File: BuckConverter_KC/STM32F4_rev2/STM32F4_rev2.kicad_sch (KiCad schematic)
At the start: 50 parts, among them J1 Screw_Terminal_01x02, J2 SWD, J3 Conn_01x04, J4 Conn_01x04, J5 USB_B_Micro, Q1 AO3401A, SW1 SW_SPDT, U1 MP2359DJ-LF-Z, U2 STM32F405RGTy, U3 USBLC6-2SC6, Y1 16Mhz

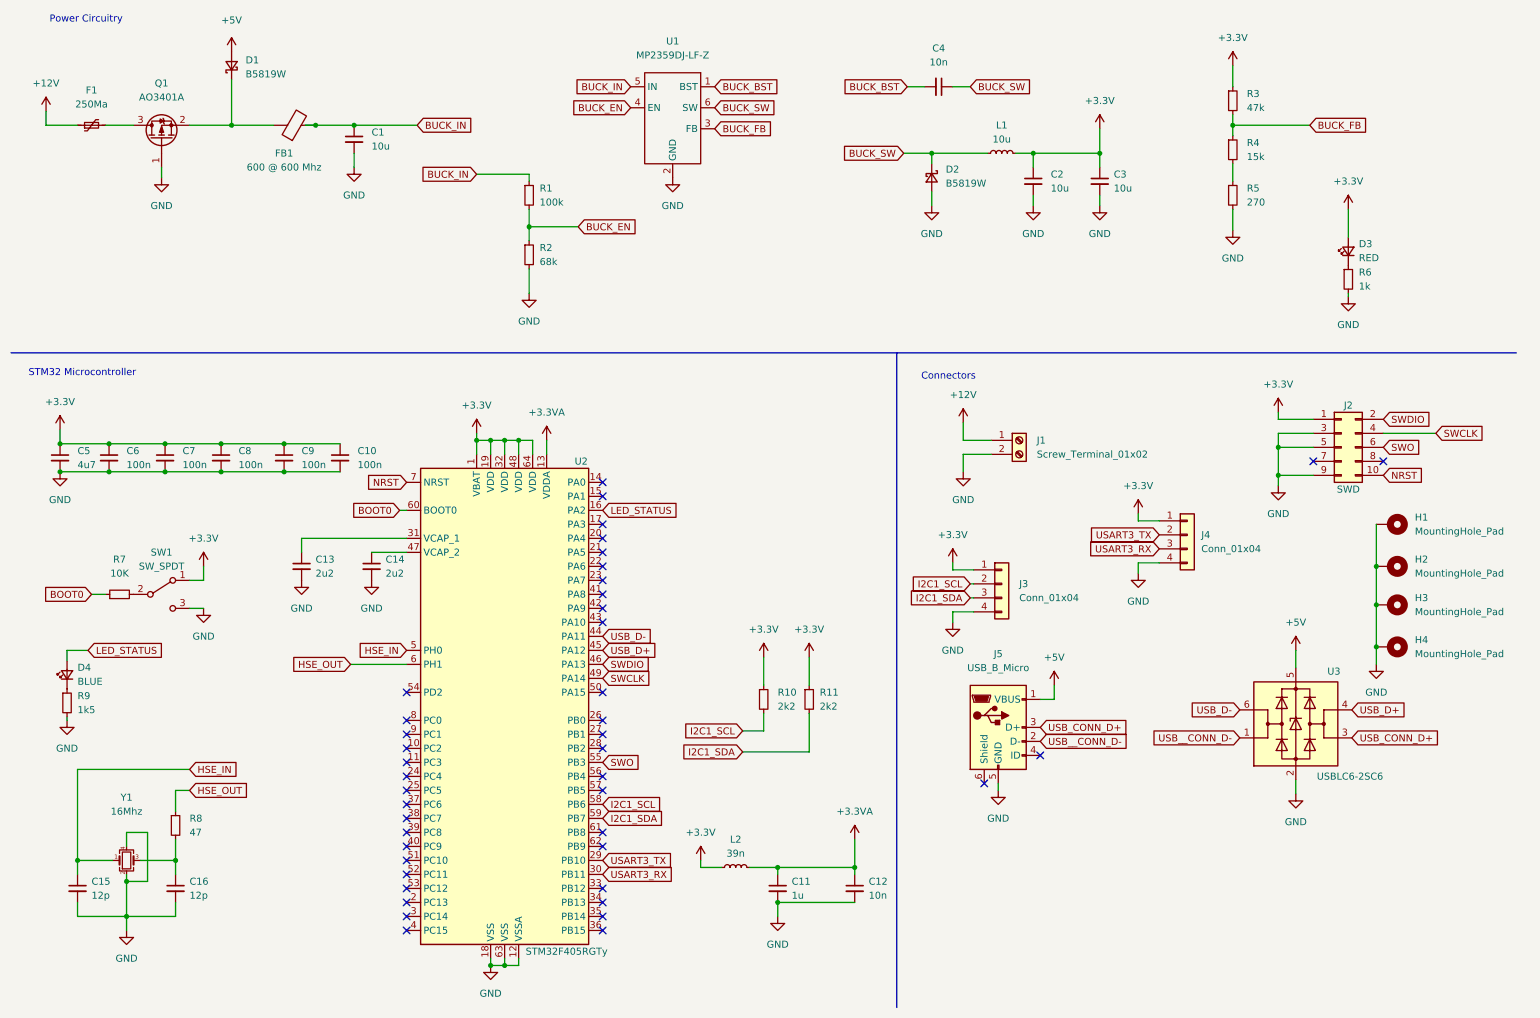
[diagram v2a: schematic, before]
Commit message: finished layout less the 3v3 and gnd
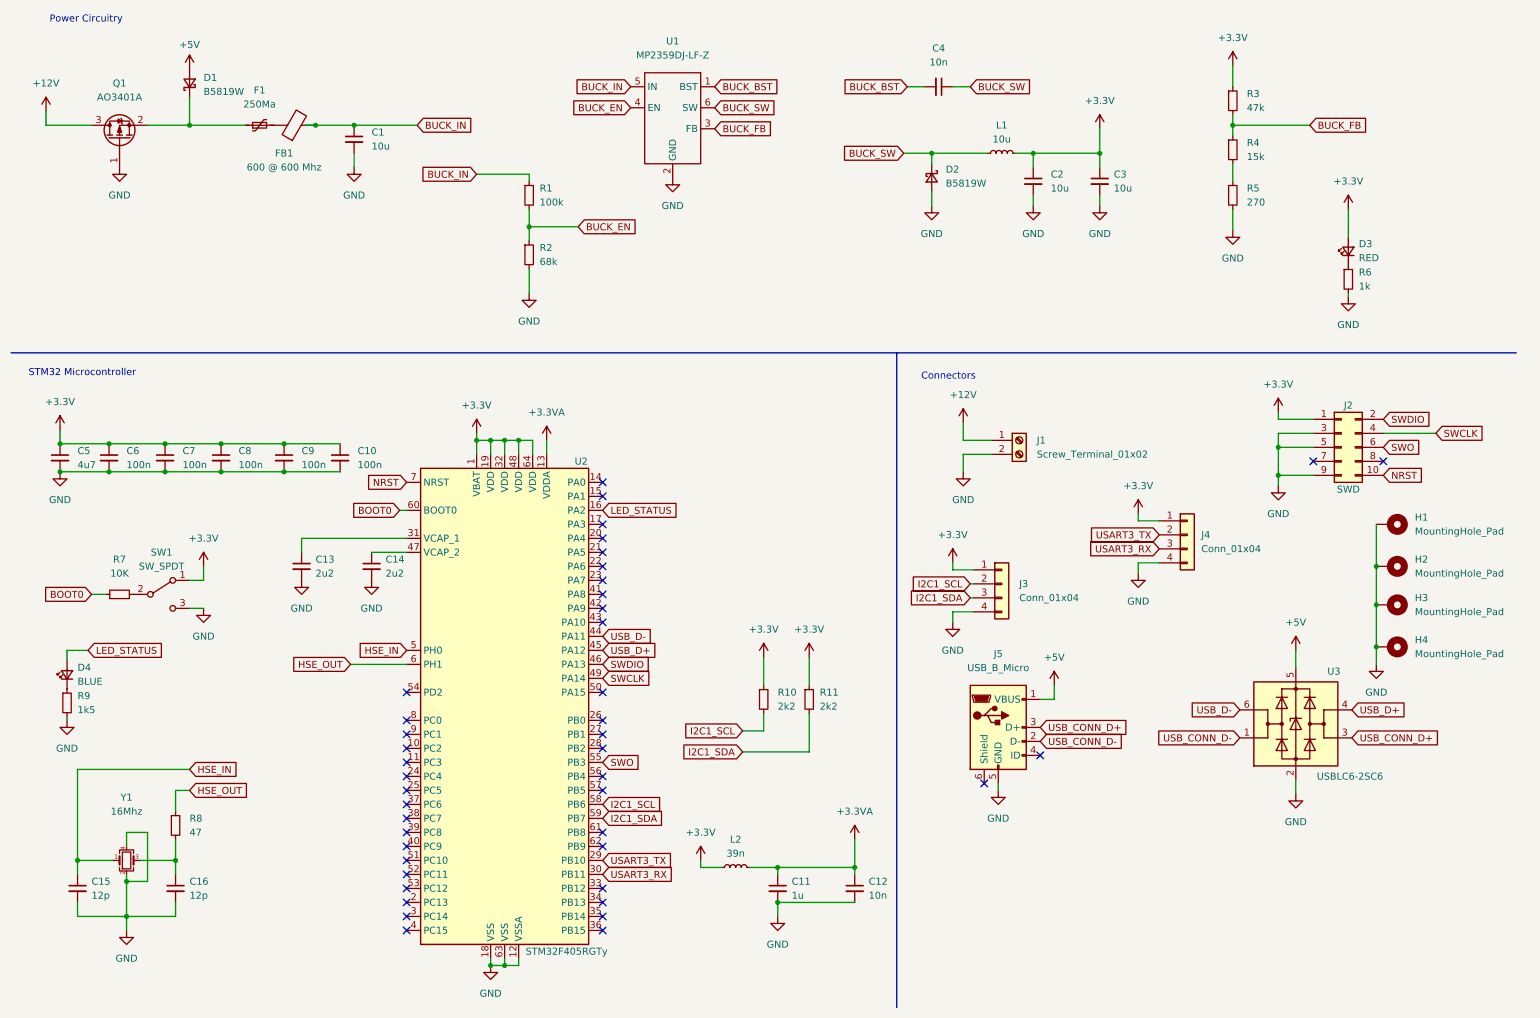
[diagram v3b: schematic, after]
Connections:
- net +12V: now also Q1.3 (D); no longer F1.1
- net at D1.1 (K), Q1.2 (S): now also F1.1; no longer FB1.1
- net at F1.2: now also FB1.1; no longer Q1.3 (D)
- net USB__CONN_D- renamed USB_CONN_D-
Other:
- moved on the sheet: D1, F1, Q1
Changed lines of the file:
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@@
   (junction (at 61.595 100.965) (diameter 0) (color 0 0 0 0)
   )
+  (junction (at 44.45 38.1) (diameter 0) (color 0 0 0 0)
+  )
   (junction (at 29.845 100.965) (diameter 0) (color 0 0 0 0)
   )
@@
   )
   (junction (at 29.845 95.885) (diameter 0) (color 0 0 0 0)
-  )
-  (junction (at 52.07 38.1) (diameter 0) (color 0 0 0 0)
   )
   (no_connect (at 188.595 157.48))
@@
     (stroke (width 0) (type default) (color 0 0 0 0))
   )
+  (wire (pts (xy 18.415 38.1) (xy 26.67 38.1))
+    (stroke (width 0) (type default) (color 0 0 0 0))
+  )
   (wire (pts (xy 241.935 101.6) (xy 241.935 103.505))
     (stroke (width 0) (type default) (color 0 0 0 0))
@@
     (stroke (width 0) (type default) (color 0 0 0 0))
   )
+  (wire (pts (xy 44.45 38.1) (xy 54.61 38.1))
+    (stroke (width 0) (type default) (color 0 0 0 0))
+  )
   (wire (pts (xy 33.02 175.26) (xy 33.02 181.61))
     (stroke (width 0) (type default) (color 0 0 0 0))
@@
     (stroke (width 0) (type default) (color 0 0 0 0))
   )
-  (wire (pts (xy 52.07 29.845) (xy 52.07 38.1))
+  (wire (pts (xy 44.45 33.02) (xy 44.45 38.1))
+    (stroke (width 0) (type default) (color 0 0 0 0))
+  )
+  (wire (pts (xy 36.83 38.1) (xy 44.45 38.1))
     (stroke (width 0) (type default) (color 0 0 0 0))
   )
@@
     (stroke (width 0) (type default) (color 0 0 0 0))
   )
-  (wire (pts (xy 39.37 47.625) (xy 39.37 45.72))
-    (stroke (width 0) (type default) (color 0 0 0 0))
-  )
   (wire (pts (xy 259.715 110.49) (xy 259.715 118.11))
     (stroke (width 0) (type default) (color 0 0 0 0))
@@
     (stroke (width 0) (type default) (color 0 0 0 0))
   )
-  (wire (pts (xy 52.07 38.1) (xy 59.69 38.1))
-    (stroke (width 0) (type default) (color 0 0 0 0))
-  )
   (wire (pts (xy 106.68 97.79) (xy 106.68 95.25))
     (stroke (width 0) (type default) (color 0 0 0 0))
@@
     (stroke (width 0) (type default) (color 0 0 0 0))
   )
-  (wire (pts (xy 44.45 38.1) (xy 52.07 38.1))
-    (stroke (width 0) (type default) (color 0 0 0 0))
-  )
   (wire (pts (xy 233.68 27.305) (xy 233.68 31.115))
     (stroke (width 0) (type default) (color 0 0 0 0))
@@
     (stroke (width 0) (type default) (color 0 0 0 0))
   )
-  (wire (pts (xy 24.13 38.1) (xy 18.415 38.1))
-    (stroke (width 0) (type default) (color 0 0 0 0))
-  )
   (wire (pts (xy 248.285 101.6) (xy 241.935 101.6))
     (stroke (width 0) (type default) (color 0 0 0 0))
@@
   )
   (wire (pts (xy 186.69 126.365) (xy 182.88 126.365))
-    (stroke (width 0) (type default) (color 0 0 0 0))
-  )
-  (wire (pts (xy 34.29 38.1) (xy 29.21 38.1))
     (stroke (width 0) (type default) (color 0 0 0 0))
   )
@@
     )
   )
-  (global_label "USB__CONN_D-" (shape input) (at 198.755 149.86 0) (fields_autoplaced)
-    (effects (font (size 1.27 1.27)) (justify left))
-    (property "Intersheet References" "${INTERSHEET_REFS}" (id 0) (at 215.9848 149.7806 0)
+  (global_label "USB_CONN_D-" (shape input) (at 198.755 149.86 0) (fields_autoplaced)
+    (effects (font (size 1.27 1.27)) (justify left))
+    (property "Intersheet References" "${INTERSHEET_REFS}" (id 0) (at 215.0171 149.7806 0)
       (effects (font (size 1.27 1.27)) (justify left) hide)
     )
@@
     )
   )
-  (global_label "USB__CONN_D-" (shape input) (at 234.95 149.225 180) (fields_autoplaced)
+  (global_label "USB_CONN_D-" (shape input) (at 234.95 149.225 180) (fields_autoplaced)
     (effects (font (size 1.27 1.27)) (justify right))
-    (property "Intersheet References" "${INTERSHEET_REFS}" (id 0) (at 217.7202 149.3044 0)
+    (property "Intersheet References" "${INTERSHEET_REFS}" (id 0) (at 218.6879 149.1456 0)
       (effects (font (size 1.27 1.27)) (justify right) hide)
     )
@@
     (pin "1")
   )
-  (symbol (lib_id "power:+5V") (at 52.07 24.765 0) (unit 1)
-    (in_bom yes) (on_board yes) (fields_autoplaced)
-    (property "Reference" "#PWR0104" (id 0) (at 52.07 28.575 0)
-      (effects (font (size 1.27 1.27)) hide)
-    )
-    (property "Value" "+5V" (id 1) (at 52.07 19.05 0))
-    (property "Footprint" "" (id 2) (at 52.07 24.765 0)
-      (effects (font (size 1.27 1.27)) hide)
-    )
-    (property "Datasheet" "" (id 3) (at 52.07 24.765 0)
+  (symbol (lib_id "power:+5V") (at 44.45 27.94 0) (unit 1)
+    (in_bom yes) (on_board yes)
+    (property "Reference" "#PWR0104" (id 0) (at 44.45 31.75 0)
+      (effects (font (size 1.27 1.27)) hide)
+    )
+    (property "Value" "+5V" (id 1) (at 44.45 23.495 0))
+    (property "Footprint" "" (id 2) (at 44.45 27.94 0)
+      (effects (font (size 1.27 1.27)) hide)
+    )
+    (property "Datasheet" "" (id 3) (at 44.45 27.94 0)
       (effects (font (size 1.27 1.27)) hide)
     )
@@
     (pin "2")
   )
-  (symbol (lib_id "Device:D_Schottky_Small") (at 52.07 27.305 90) (unit 1)
-    (in_bom yes) (on_board yes) (fields_autoplaced)
-    (property "Reference" "D1" (id 0) (at 54.61 26.2889 90)
+  (symbol (lib_id "Device:D_Schottky_Small") (at 44.45 30.48 90) (unit 1)
+    (in_bom yes) (on_board yes) (fields_autoplaced)
+    (property "Reference" "D1" (id 0) (at 46.99 29.4639 90)
       (effects (font (size 1.27 1.27)) (justify right))
     )
-    (property "Value" "B5819W" (id 1) (at 54.61 28.8289 90)
+    (property "Value" "B5819W" (id 1) (at 46.99 32.0039 90)
       (effects (font (size 1.27 1.27)) (justify right))
     )
-    (property "Footprint" "Diode_SMD:D_SOD-123" (id 2) (at 52.07 27.305 90)
-      (effects (font (size 1.27 1.27)) hide)
-    )
-    (property "Datasheet" "~" (id 3) (at 52.07 27.305 90)
+    (property "Footprint" "Diode_SMD:D_SOD-123" (id 2) (at 44.45 30.48 90)
+      (effects (font (size 1.27 1.27)) hide)
+    )
+    (property "Datasheet" "~" (id 3) (at 44.45 30.48 90)
       (effects (font (size 1.27 1.27)) hide)
     )
@@
     (pin "2")
   )
-  (symbol (lib_id "Device:Polyfuse_Small") (at 26.67 38.1 90) (unit 1)
-    (in_bom yes) (on_board yes) (fields_autoplaced)
-    (property "Reference" "F1" (id 0) (at 26.67 31.75 90))
-    (property "Value" "250Ma" (id 1) (at 26.67 34.29 90))
-    (property "Footprint" "Fuse:Fuse_1206_3216Metric" (id 2) (at 31.75 36.83 0)
-      (effects (font (size 1.27 1.27)) (justify left) hide)
-    )
-    (property "Datasheet" "~" (id 3) (at 26.67 38.1 0)
+  (symbol (lib_id "Device:Polyfuse_Small") (at 57.15 38.1 90) (unit 1)
+    (in_bom yes) (on_board yes) (fields_autoplaced)
+    (property "Reference" "F1" (id 0) (at 57.15 31.75 90))
+    (property "Value" "250Ma" (id 1) (at 57.15 34.29 90))
+    (property "Footprint" "Fuse:Fuse_1206_3216Metric" (id 2) (at 62.23 36.83 0)
+      (effects (font (size 1.27 1.27)) (justify left) hide)
+    )
+    (property "Datasheet" "~" (id 3) (at 57.15 38.1 0)
       (effects (font (size 1.27 1.27)) hide)
     )
@@
     (pin "1")
   )
-  (symbol (lib_id "Transistor_FET:AO3401A") (at 39.37 40.64 90) (unit 1)
-    (in_bom yes) (on_board yes) (fields_autoplaced)
-    (property "Reference" "Q1" (id 0) (at 39.37 30.48 90))
-    (property "Value" "AO3401A" (id 1) (at 39.37 33.02 90))
-    (property "Footprint" "Package_TO_SOT_SMD:SOT-23" (id 2) (at 41.275 35.56 0)
+  (symbol (lib_id "Transistor_FET:AO3401A") (at 31.75 40.64 90) (unit 1)
+    (in_bom yes) (on_board yes) (fields_autoplaced)
+    (property "Reference" "Q1" (id 0) (at 31.75 30.48 90))
+    (property "Value" "AO3401A" (id 1) (at 31.75 33.02 90))
+    (property "Footprint" "Package_TO_SOT_SMD:SOT-23" (id 2) (at 33.655 35.56 0)
       (effects (font (size 1.27 1.27) italic) (justify left) hide)
     )
-    (property "Datasheet" "http://www.aosmd.com/pdfs/datasheet/AO3401A.pdf" (id 3) (at 39.37 40.64 0)
+    (property "Datasheet" "http://www.aosmd.com/pdfs/datasheet/AO3401A.pdf" (id 3) (at 31.75 40.64 0)
       (effects (font (size 1.27 1.27)) (justify left) hide)
     )
@@
     (pin "4")
   )
-  (symbol (lib_id "power:GND") (at 39.37 47.625 0) (unit 1)
-    (in_bom yes) (on_board yes) (fields_autoplaced)
-    (property "Reference" "#PWR0103" (id 0) (at 39.37 53.975 0)
-      (effects (font (size 1.27 1.27)) hide)
-    )
-    (property "Value" "GND" (id 1) (at 39.37 52.705 0))
-    (property "Footprint" "" (id 2) (at 39.37 47.625 0)
-      (effects (font (size 1.27 1.27)) hide)
-    )
-    (property "Datasheet" "" (id 3) (at 39.37 47.625 0)
-      (effects (font (size 1.27 1.27)) hide)
-    )
+  (symbol (lib_id "power:GND") (at 31.75 45.72 0) (unit 1)
+    (in_bom yes) (on_board yes) (fields_autoplaced)
+    (property "Reference" "#PWR0103" (id 0) (at 31.75 52.07 0)
+      (effects (font (size 1.27 1.27)) hide)
+    )
+    (property "Value" "GND" (id 1) (at 31.75 50.8 0))
+    (property "Footprint" "" (id 2) (at 31.75 45.72 0)
+      (effects (font (size 1.27 1.27)) hide)
+    )
+    (property "Datasheet" "" (id 3) (at 31.75 45.72 0)
+      (effects (font (size 1.27 1.27)) hide)
+    )

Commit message: finished layout; generated gerber, component footprints position files, BOM
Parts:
- J2: footprint Connector_PinSocket_1.27mm:PinSocket_2x05_P1.27mm_Vertical_SMD -> Connector_PinHeader_1.27mm:PinHeader_2x05_P1.27mm_Vertical_SMD
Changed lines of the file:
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@@
     (property "Reference" "J2" (id 0) (at 254.635 88.9 0))
     (property "Value" "SWD" (id 1) (at 254.635 104.14 0))
-    (property "Footprint" "Connector_PinSocket_1.27mm:PinSocket_2x05_P1.27mm_Vertical_SMD" (id 2) (at 253.365 96.52 0)
+    (property "Footprint" "Connector_PinHeader_1.27mm:PinHeader_2x05_P1.27mm_Vertical_SMD" (id 2) (at 253.365 96.52 0)
       (effects (font (size 1.27 1.27)) hide)
     )
@@
     )
     (path "/d129bde9-fd8d-4210-99d7-cc8d47c9926e"
-      (reference "J2") (unit 1) (value "SWD") (footprint "Connector_PinSocket_1.27mm:PinSocket_2x05_P1.27mm_Vertical_SMD")
+      (reference "J2") (unit 1) (value "SWD") (footprint "Connector_PinHeader_1.27mm:PinHeader_2x05_P1.27mm_Vertical_SMD")
     )
     (path "/9d7bd142-a6ca-4b80-bdec-a5f7969ab7b5"
